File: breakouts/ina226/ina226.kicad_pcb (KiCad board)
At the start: 2 copper layers, 26.8 x 18.2 mm, 13 parts, among them J1 Conn_01x05_Pin, J2 Screw_Terminal_01x02, U1 INA226

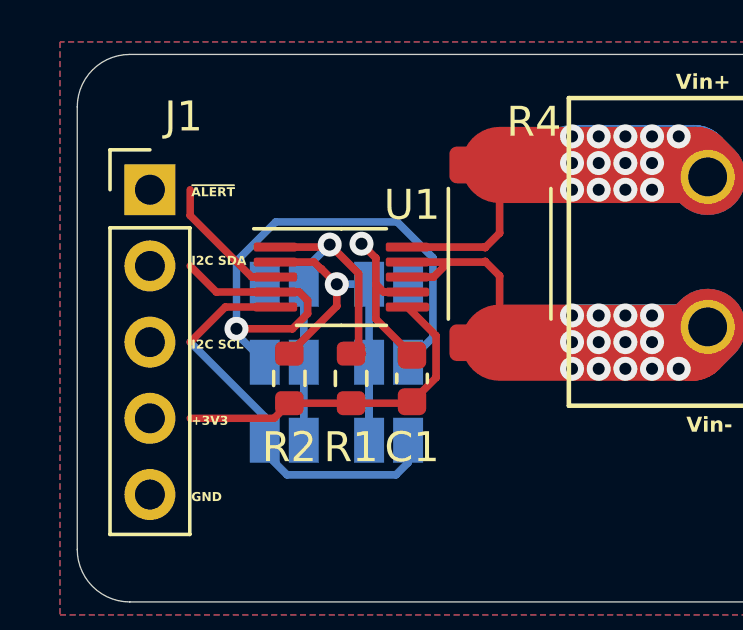
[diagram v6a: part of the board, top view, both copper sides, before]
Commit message: Feat[breakouts]: Fixed wiring, 3d model broken
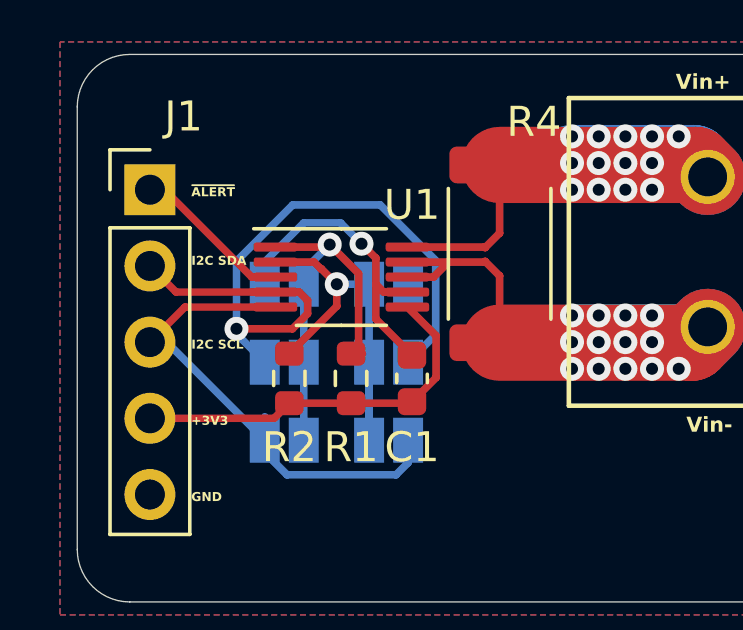
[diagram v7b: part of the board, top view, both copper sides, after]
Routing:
- net GND: track 5.57 -> 10.4 mm
- net /I2C SCL: track 14.0 -> 17.0 mm
- net /I2C SDA: track 23.5 -> 25.4 mm
- net +3V3: track 11.5 -> 12.8 mm
- net /~{ALERT}: track 4.55 -> 5.39 mm
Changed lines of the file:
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@@
   (segment (start 145.712434 83.4213) (end 145.45395 83.162816) (width 0.254) (layer "F.Cu") (net 1))
   (via (at 144.974964 81.8101) (size 0.8) (drill 0.4) (layers "F.Cu" "B.Cu") (net 1))
+  (segment (start 141.75155 82.4096) (end 143.04735 81.1138) (width 0.25) (layer "B.Cu") (net 1))
+  (segment (start 144.278664 81.1138) (end 144.974964 81.8101) (width 0.25) (layer "B.Cu") (net 1))
+  (segment (start 141.75155 83.1596) (end 141.75155 82.4096) (width 0.25) (layer "B.Cu") (net 1))
+  (segment (start 143.04735 81.1138) (end 144.278664 81.1138) (width 0.25) (layer "B.Cu") (net 1))
+  (segment (start 142.06395 87.63) (end 142.56895 87.125) (width 0.25) (layer "F.Cu") (net 2))
   (segment (start 147.46035 84.8757) (end 147.46035 86.273) (width 0.254) (layer "F.Cu") (net 2))
   (segment (start 147.46035 86.273) (end 146.65835 87.075) (width 0.254) (layer "F.Cu") (net 2))
-  (segment (start 142.06395 87.63) (end 142.56895 87.125) (width 0.25) (layer "F.Cu") (net 2))
-  (segment (start 139.26435 87.63) (end 142.06395 87.63) (width 0.25) (layer "F.Cu") (net 2))
+  (segment (start 137.922 87.63) (end 142.06395 87.63) (width 0.25) (layer "F.Cu") (net 2))
   (segment (start 146.60835 87.125) (end 146.65835 87.075) (width 0.25) (layer "F.Cu") (net 2))
   (segment (start 142.56895 87.125) (end 144.62635 87.125) (width 0.25) (layer "F.Cu") (net 2))
   (segment (start 146.50595 83.9213) (end 147.46035 84.8757) (width 0.254) (layer "F.Cu") (net 2))
   (segment (start 144.62635 87.125) (end 146.60835 87.125) (width 0.25) (layer "F.Cu") (net 2))
-  (segment (start 139.26435 85.09) (end 140.43305 83.9213) (width 0.25) (layer "F.Cu") (net 3))
-  (segment (start 140.43305 83.9213) (end 142.10595 83.9213) (width 0.25) (layer "F.Cu") (net 3))
-  (segment (start 141.75155 87.5772) (end 139.26435 85.09) (width 0.254) (layer "B.Cu") (net 3))
+  (segment (start 137.922 85.09) (end 139.0907 83.9213) (width 0.25) (layer "F.Cu") (net 3))
+  (segment (start 139.0907 83.9213) (end 142.10595 83.9213) (width 0.25) (layer "F.Cu") (net 3))
   (segment (start 146.12508 89.513266) (end 146.528746 89.1096) (width 0.254) (layer "B.Cu") (net 3))
   (segment (start 141.75155 88.3596) (end 141.75155 87.5772) (width 0.254) (layer "B.Cu") (net 3))
+  (segment (start 138.48195 85.09) (end 137.922 85.09) (width 0.254) (layer "B.Cu") (net 3))
   (segment (start 141.75155 88.77205) (end 142.492766 89.513266) (width 0.254) (layer "B.Cu") (net 3))
   (segment (start 141.75155 88.3596) (end 141.75155 88.77205) (width 0.254) (layer "B.Cu") (net 3))
   (segment (start 146.528746 89.1096) (end 146.528746 88.3596) (width 0.254) (layer "B.Cu") (net 3))
   (segment (start 142.492766 89.513266) (end 146.12508 89.513266) (width 0.254) (layer "B.Cu") (net 3))
+  (segment (start 141.75155 88.3596) (end 138.48195 85.09) (width 0.254) (layer "B.Cu") (net 3))
   (segment (start 143.17855 83.700384) (end 142.899466 83.4213) (width 0.254) (layer "F.Cu") (net 4))
   (segment (start 142.674966 84.6458) (end 143.17855 84.142216) (width 0.254) (layer "F.Cu") (net 4))
-  (segment (start 140.13565 83.4213) (end 142.10595 83.4213) (width 0.25) (layer "F.Cu") (net 4))
+  (segment (start 138.7933 83.4213) (end 142.10595 83.4213) (width 0.25) (layer "F.Cu") (net 4))
   (segment (start 143.17855 84.142216) (end 143.17855 83.700384) (width 0.254) (layer "F.Cu") (net 4))
-  (segment (start 139.26435 82.55) (end 140.13565 83.4213) (width 0.25) (layer "F.Cu") (net 4))
   (segment (start 142.899466 83.4213) (end 142.10595 83.4213) (width 0.254) (layer "F.Cu") (net 4))
+  (segment (start 137.922 82.55) (end 138.7933 83.4213) (width 0.25) (layer "F.Cu") (net 4))
   (segment (start 140.807303 84.6458) (end 142.674966 84.6458) (width 0.254) (layer "F.Cu") (net 4))
   (segment (start 141.312434 83.4213) (end 142.10595 83.4213) (width 0.254) (layer "F.Cu") (net 4))
   (via (at 140.807303 84.6458) (size 0.8) (drill 0.4) (layers "F.Cu" "B.Cu") (net 4))
-  (segment (start 146.164696 81.0831) (end 147.355746 82.27415) (width 0.254) (layer "B.Cu") (net 4))
+  (segment (start 140.807303 84.815353) (end 141.75155 85.7596) (width 0.254) (layer "B.Cu") (net 4))
   (segment (start 140.807303 84.6458) (end 140.807303 82.391397) (width 0.254) (layer "B.Cu") (net 4))
-  (segment (start 140.807303 82.391397) (end 142.1156 81.0831) (width 0.254) (layer "B.Cu") (net 4))
-  (segment (start 140.807303 84.815353) (end 141.75155 85.7596) (width 0.254) (layer "B.Cu") (net 4))
-  (segment (start 147.355746 84.9326) (end 146.528746 85.7596) (width 0.254) (layer "B.Cu") (net 4))
+  (segment (start 140.807303 82.391397) (end 142.6807 80.518) (width 0.254) (layer "B.Cu") (net 4))
+  (segment (start 147.447 84.841346) (end 146.528746 85.7596) (width 0.254) (layer "B.Cu") (net 4))
   (segment (start 140.807303 84.6458) (end 140.807303 84.815353) (width 0.254) (layer "B.Cu") (net 4))
+  (segment (start 145.599596 80.518) (end 147.447 82.365404) (width 0.254) (layer "B.Cu") (net 4))
+  (segment (start 142.6807 80.518) (end 145.599596 80.518) (width 0.254) (layer "B.Cu") (net 4))
+  (segment (start 147.447 82.365404) (end 147.447 84.841346) (width 0.254) (layer "B.Cu") (net 4))
   (segment (start 141.75155 85.590047) (end 141.75155 85.7596) (width 0.254) (layer "B.Cu") (net 4))
-  (segment (start 142.1156 81.0831) (end 146.164696 81.0831) (width 0.254) (layer "B.Cu") (net 4))
-  (segment (start 147.355746 82.27415) (end 147.355746 84.9326) (width 0.254) (layer "B.Cu") (net 4))
   (segment (start 149.07765 81.9213) (end 149.09675 81.9404) (width 0.254) (layer "F.Cu") (net 5))
   (segment (start 146.50595 81.9213) (end 149.07765 81.9213) (width 0.254) (layer "F.Cu") (net 5))
@@
   (segment (start 156.00555 85.09) (end 156.51355 84.582) (width 2.54) (layer "B.Cu") (net 6))
   (segment (start 151.99235 85.09) (end 156.00555 85.09) (width 2.54) (layer "B.Cu") (net 6))
-  (segment (start 139.26435 80.870386) (end 141.315264 82.9213) (width 0.25) (layer "F.Cu") (net 7))
-  (segment (start 139.26435 80.01) (end 139.26435 80.870386) (width 0.25) (layer "F.Cu") (net 7))
+  (segment (start 138.403964 80.01) (end 141.315264 82.9213) (width 0.25) (layer "F.Cu") (net 7))
+  (segment (start 137.922 80.01) (end 138.403964 80.01) (width 0.25) (layer "F.Cu") (net 7))
   (segment (start 141.315264 82.9213) (end 142.10595 82.9213) (width 0.25) (layer "F.Cu") (net 7))
   (segment (start 144.87805 82.8017) (end 144.87805 85.2233) (width 0.254) (layer "F.Cu") (net 8))

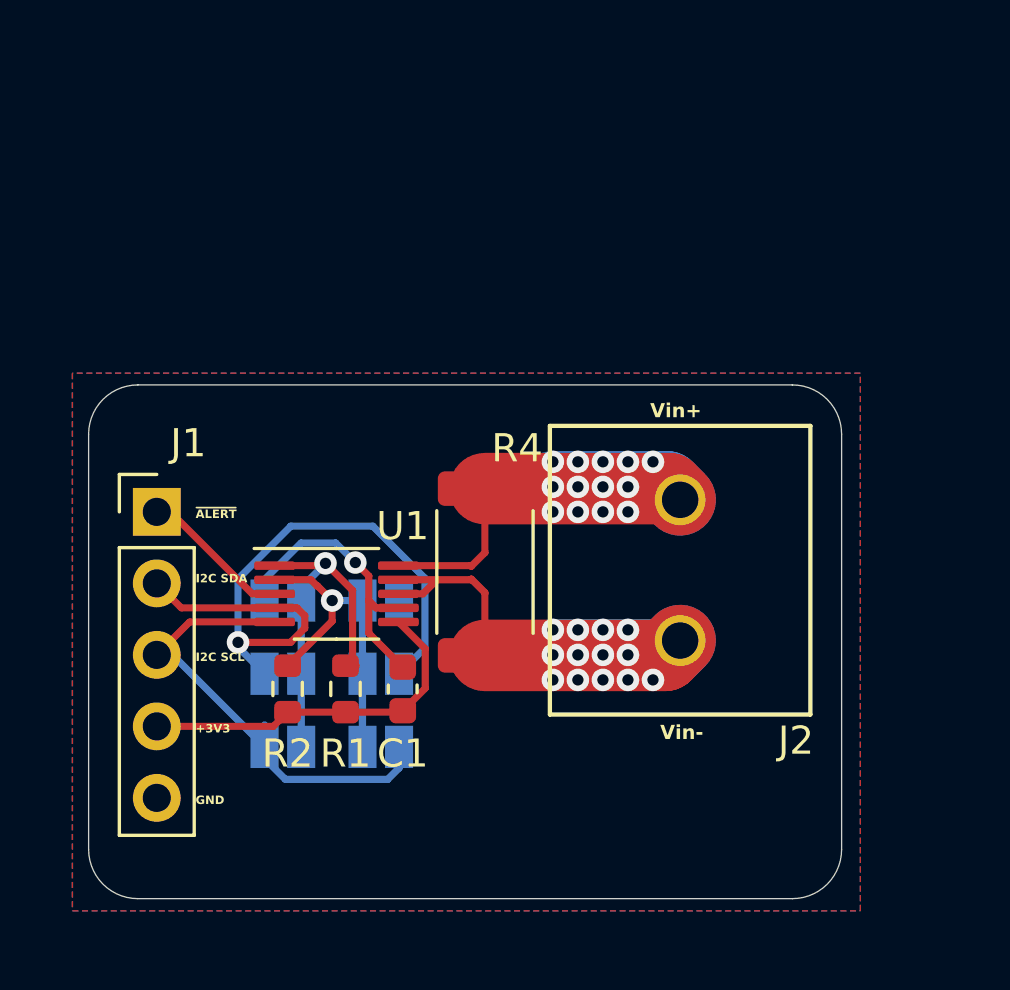
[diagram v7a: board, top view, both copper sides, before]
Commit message: Feat[breakouts]: Fixed silk, increased board size
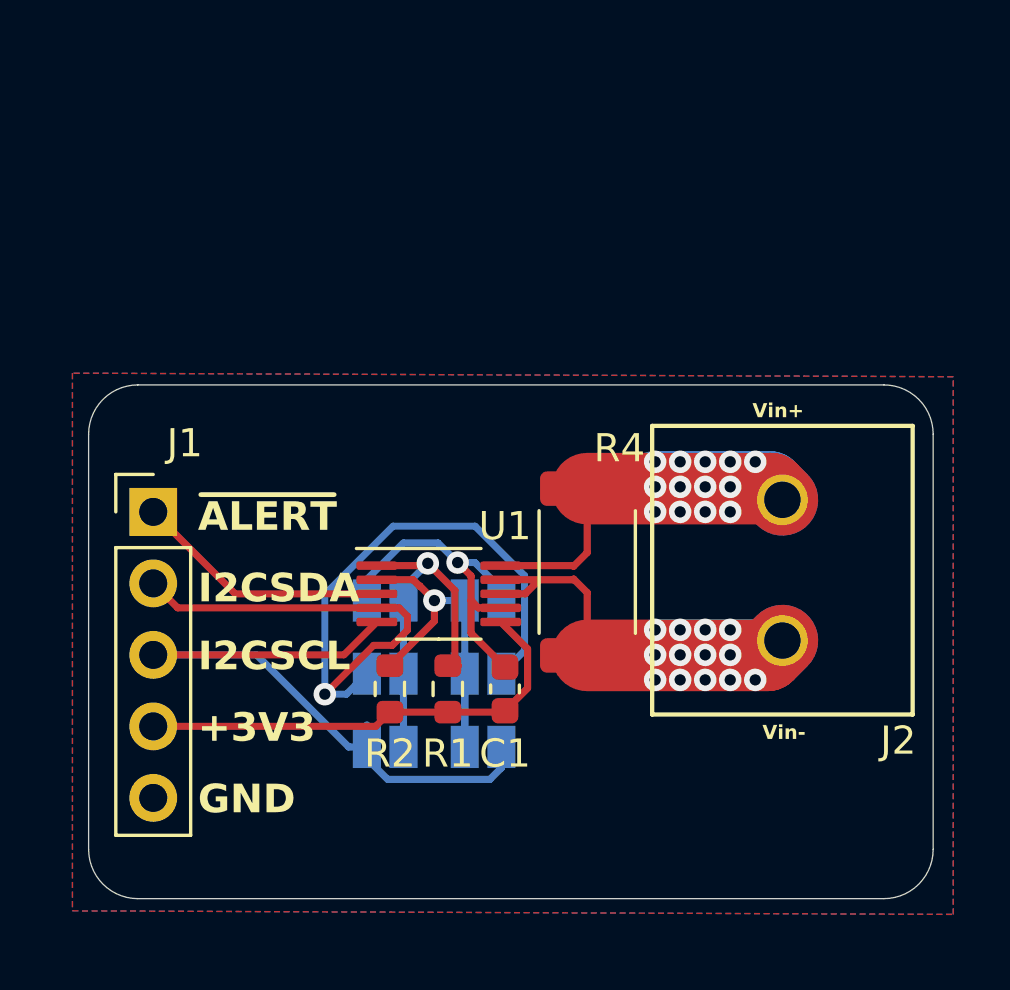
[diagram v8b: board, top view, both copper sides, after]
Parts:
- moved JP1 3.63 mm to (146.0, 83.2)
- moved JP2 3.63 mm to (146.0, 85.8)
- moved JP3 3.63 mm to (146.0, 88.4)
- moved R1 3.63 mm to (148.3, 86.3)
- moved R2 3.63 mm to (146.2, 86.3)
- moved U1 3.63 mm to (147.9, 82.9)
- moved C1 3.63 mm to (150.3, 86.3)
- moved J2 3.63 mm to (160.1, 84.6)
- moved JP4 3.63 mm to (149.5, 83.2)
- moved JP5 3.63 mm to (149.5, 85.8)
- moved JP6 3.63 mm to (149.5, 88.4)
- moved R4 3.63 mm to (153.2, 82.1)
- moved J1 0.13 mm to (137.8, 80.0)
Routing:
- net /I2C SCL: track 17.0 -> 24.6 mm
- net /I2C SDA: track 25.4 -> 32.0 mm
- net /~{ALERT}: track 5.39 -> 9.63 mm
- net +3V3: track 12.8 -> 16.6 mm
- net GND: track 10.4 -> 12.7 mm
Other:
- board size 26.8 x 18.2 mm -> 30 x 18.2 mm
- board text added: "I2CSCL"
- board text added: "I2CSDA"
- board text removed: "I2C SCL"
- board text removed: "I2C SDA"
